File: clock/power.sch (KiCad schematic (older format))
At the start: 51 parts

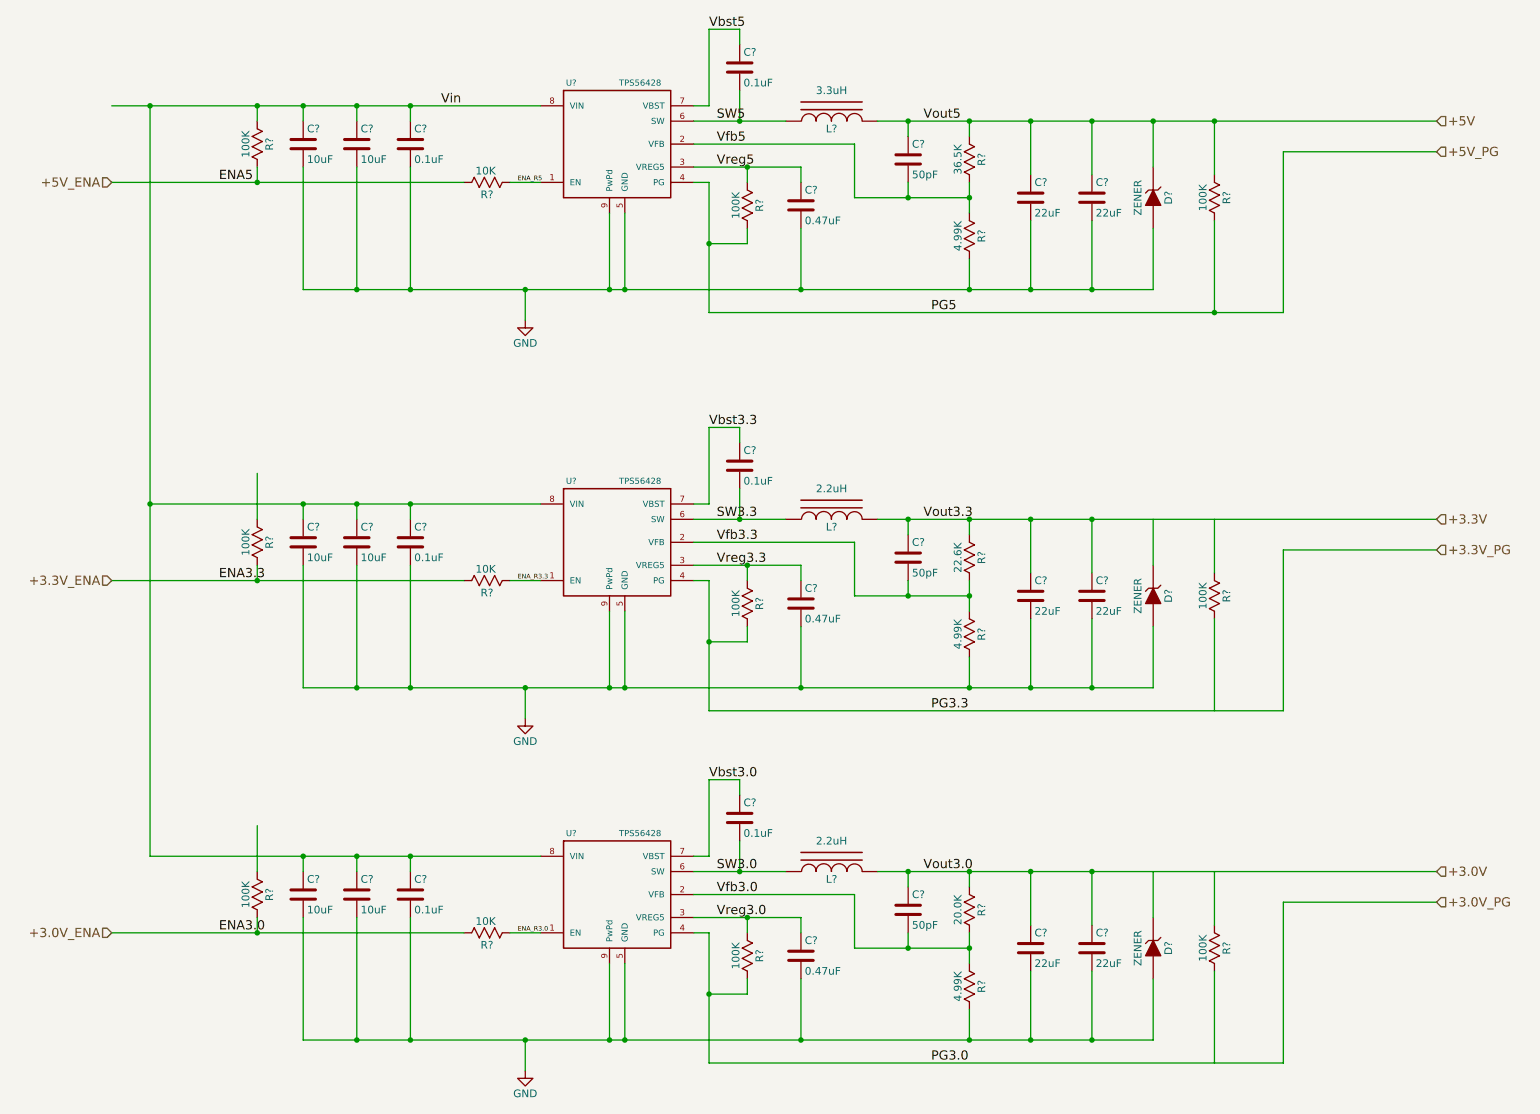
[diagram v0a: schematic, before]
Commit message: Fill in some of the BOM entries.
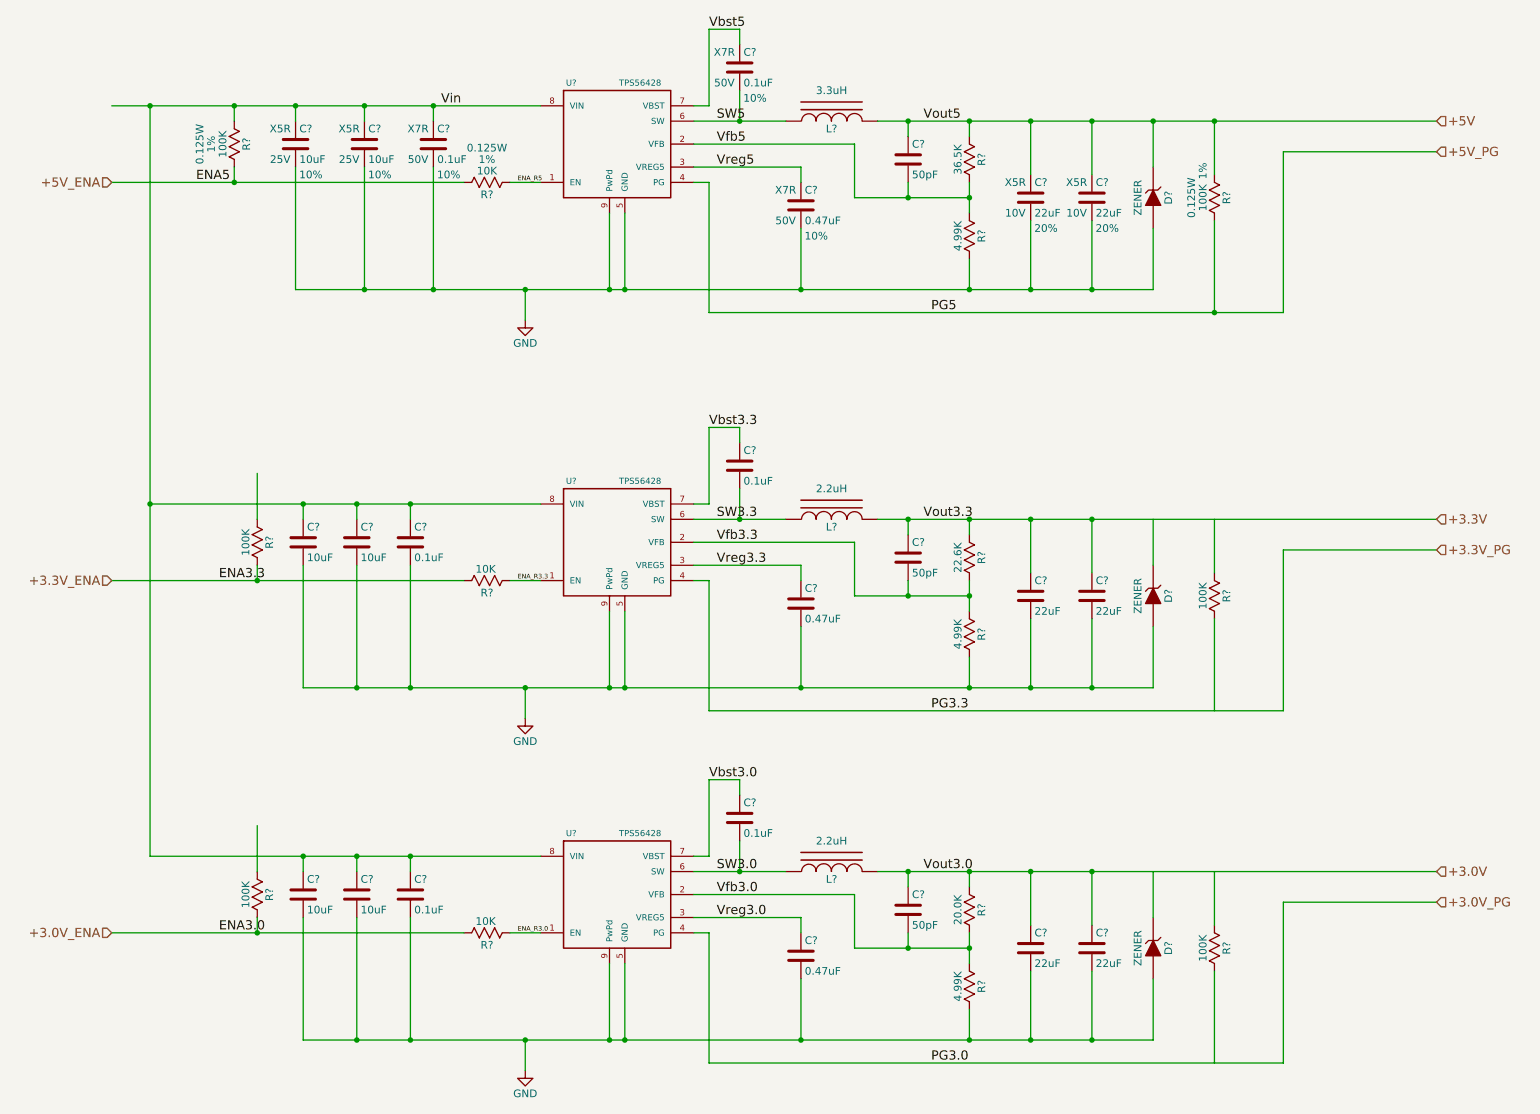
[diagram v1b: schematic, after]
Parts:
- removed C? (x2): 10uF, Capacitors_SMD:C_1206_HandSoldering, symbol C
- removed C? (x2): 0.1uF, Capacitors_SMD:C_0805_HandSoldering, symbol C
- removed C?: 0.47uF, Capacitors_SMD:C_0805_HandSoldering, symbol C
- removed C? (x2): 22uF, Capacitors_SMD:C_1206_HandSoldering, symbol C
- removed R? (x5): 100K, symbol R_local
- removed R?: 10K, symbol R_local
- removed U?: TPS56428, symbol TPS56428
- added C? (x2): 10uF, Capacitors_SMD:C_1206_HandSoldering, symbol C
- added C? (x2): 0.1uF, Capacitors_SMD:C_0805_HandSoldering, symbol C
- added C? (x2): 22uF, Capacitors_SMD:C_1206_HandSoldering, symbol C
- added C?: 0.47uF, Capacitors_SMD:C_0805_HandSoldering, symbol C
- added R? (x2): 100K, Resistors_SMD:R_0805_HandSoldering, symbol R_local
- added R?: 10K, Resistors_SMD:R_0805_HandSoldering, symbol R_local
- added U?: TPS56428, symbol TPS56428
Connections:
- wire segments 148 -> 139

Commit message: Update parts with parameter detail and BOM information.
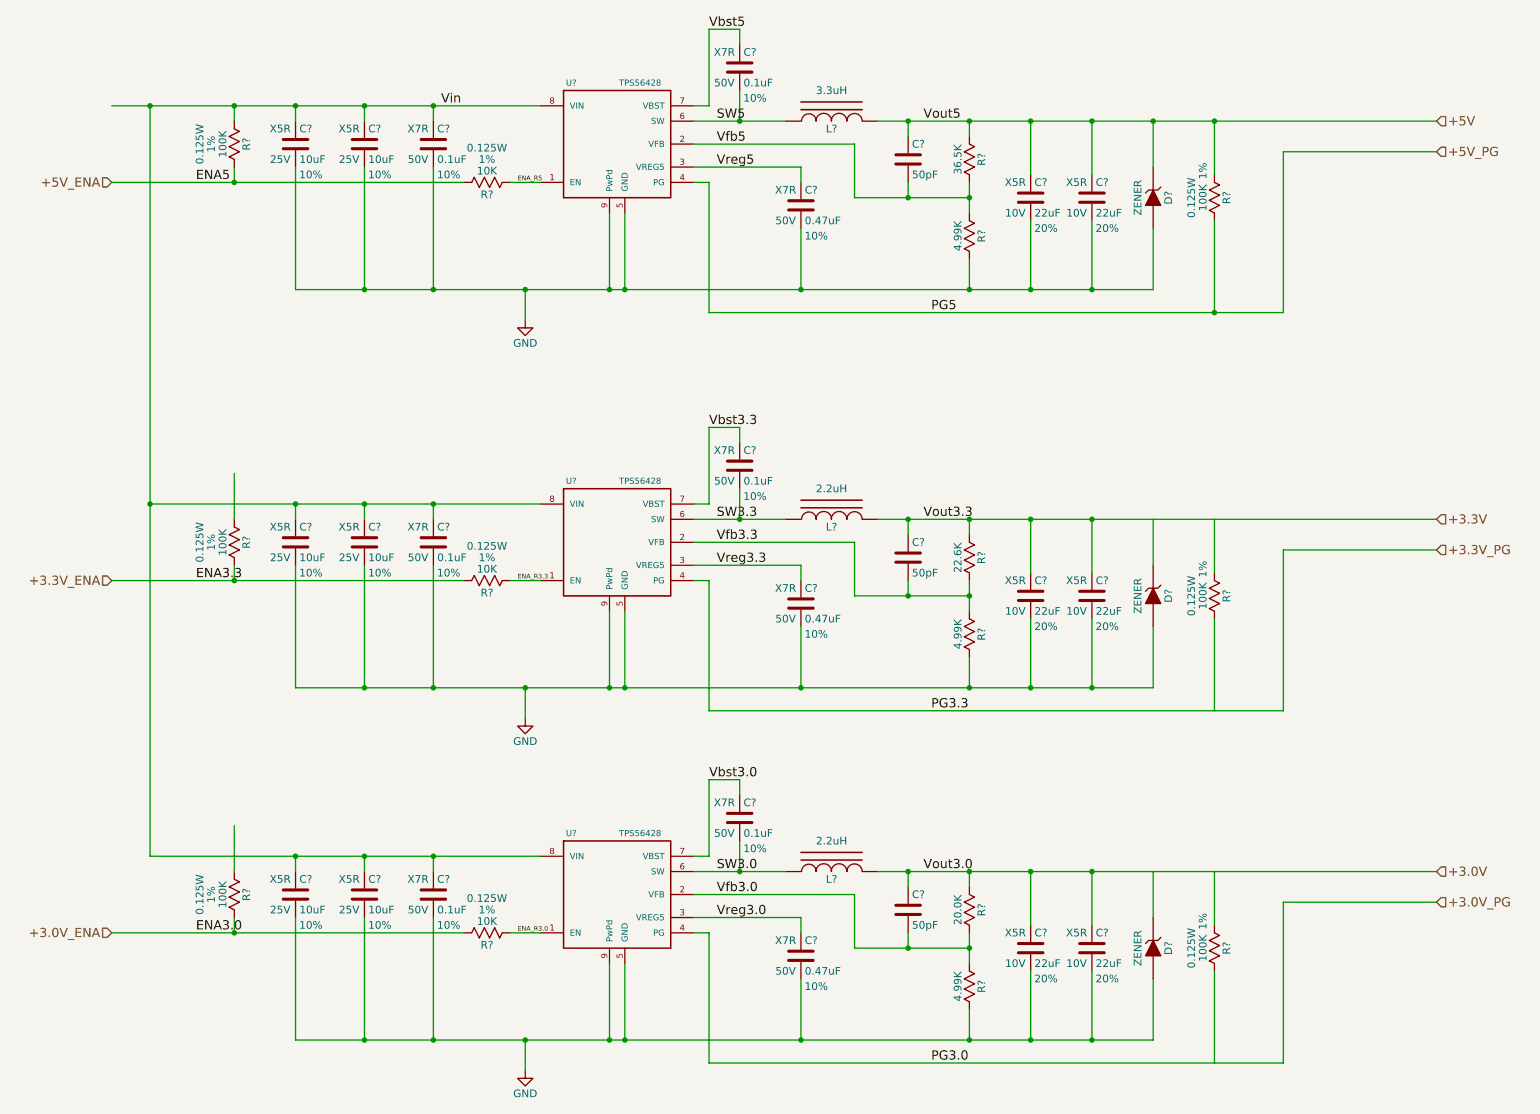
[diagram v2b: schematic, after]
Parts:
- removed C? (x4): 10uF, Capacitors_SMD:C_1206_HandSoldering, symbol C
- removed C? (x4): 0.1uF, Capacitors_SMD:C_0805_HandSoldering, symbol C
- removed C? (x2): 0.47uF, Capacitors_SMD:C_0805_HandSoldering, symbol C
- removed C? (x4): 22uF, Capacitors_SMD:C_1206_HandSoldering, symbol C
- removed R? (x4): 100K, symbol R_local
- removed R? (x2): 10K, symbol R_local
- removed U? (x2): TPS56428, symbol TPS56428
- added C? (x4): 10uF, Capacitors_SMD:C_1206_HandSoldering, symbol C
- added C? (x4): 0.1uF, Capacitors_SMD:C_0805_HandSoldering, symbol C
- added C? (x2): 0.47uF, Capacitors_SMD:C_0805_HandSoldering, symbol C
- added C? (x4): 22uF, Capacitors_SMD:C_1206_HandSoldering, symbol C
- added R? (x2): 10K, Resistors_SMD:R_0805_HandSoldering, symbol R_local
- added R? (x4): 100K, Resistors_SMD:R_0805_HandSoldering, symbol R_local
- added U? (x2): TPS56428, symbol TPS56428
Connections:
- wire segments 139 -> 205

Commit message: Add parameter for RF connector. Start adding display connections.
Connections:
- wire segments 205 -> 139
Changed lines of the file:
@@
 $EndComp
 Wire Wire Line
-	8500 2350 8700 2350
-Wire Wire Line
-	8700 2350 9100 2350
-Wire Wire Line
-	9100 2350 9500 2350
-Wire Wire Line
-	9500 2350 9900 2350
-Wire Wire Line
-	9900 2350 10300 2350
-Wire Wire Line
-	10300 2350 10700 2350
-Wire Wire Line
-	10700 2350 12150 2350
-Wire Wire Line
-	7300 2350 7600 2350
-Wire Wire Line
-	7600 2350 7900 2350
+	8500 2350 12150 2350
+Wire Wire Line
+	7300 2350 7900 2350
 Wire Wire Line
 	7600 2150 7600 2350
@@
 Connection ~ 9900 2350
 Wire Wire Line
-	9100 2750 9100 2850
-Wire Wire Line
-	9100 2850 9100 2950
+	9100 2750 9100 2950
 Wire Wire Line
 	6750 3450 6750 2950
@@
 	9100 3450 9100 3250
 Wire Wire Line
-	8350 2850 8700 2850
-Wire Wire Line
-	8700 2850 9100 2850
+	8350 2850 9100 2850
 Wire Wire Line
 	8350 2850 8350 2500
@@
 Connection ~ 6750 3450
 Wire Wire Line
-	3500 2250 3750 2250
-Wire Wire Line
-	3750 2250 4300 2250
-Wire Wire Line
-	4300 2250 4700 2250
-Wire Wire Line
-	4700 2250 5150 2250
-Wire Wire Line
-	5150 2250 5600 2250
-Wire Wire Line
-	5600 2250 6300 2250
+	3500 2250 6300 2250
 Wire Wire Line
 	6300 2750 6100 2750
 Wire Wire Line
-	3500 2750 4300 2750
-Wire Wire Line
-	4300 2750 5800 2750
-Wire Wire Line
-	7400 3600 10700 3600
-Wire Wire Line
-	10700 3600 11150 3600
+	3500 2750 5800 2750
+Wire Wire Line
+	7400 3600 11150 3600
 Wire Wire Line
 	6850 3450 6850 2950
@@
 $EndComp
 Wire Wire Line
-	8500 4950 8700 4950
-Wire Wire Line
-	8700 4950 9100 4950
-Wire Wire Line
-	9100 4950 9500 4950
-Wire Wire Line
-	9500 4950 9900 4950
-Wire Wire Line
-	9900 4950 12150 4950
-Wire Wire Line
-	7300 4950 7600 4950
-Wire Wire Line
-	7600 4950 7900 4950
+	8500 4950 12150 4950
+Wire Wire Line
+	7300 4950 7900 4950
 Wire Wire Line
 	7600 4750 7600 4950
@@
 Connection ~ 9900 4950
 Wire Wire Line
-	9100 5350 9100 5450
-Wire Wire Line
-	9100 5450 9100 5550
+	9100 5350 9100 5550
 Wire Wire Line
 	6750 6050 6750 5550
 Wire Wire Line
-	4700 6050 5150 6050
-Wire Wire Line
-	5150 6050 5600 6050
-Wire Wire Line
-	5600 6050 6200 6050
-Wire Wire Line
-	6200 6050 6750 6050
-Wire Wire Line
-	6750 6050 6850 6050
-Wire Wire Line
-	6850 6050 8000 6050
-Wire Wire Line
-	8000 6050 9100 6050
-Wire Wire Line
-	9100 6050 9500 6050
-Wire Wire Line
-	9500 6050 9900 6050
-Wire Wire Line
-	9900 6050 10300 6050
+	4700 6050 10300 6050
 Wire Wire Line
 	9100 6050 9100 5850
 Wire Wire Line
-	8350 5450 8700 5450
-Wire Wire Line
-	8700 5450 9100 5450
+	8350 5450 9100 5450
 Wire Wire Line
 	8350 5450 8350 5100
@@
 Connection ~ 6750 6050
 Wire Wire Line
-	3750 4850 4700 4850
-Wire Wire Line
-	4700 4850 5150 4850
-Wire Wire Line
-	5150 4850 5600 4850
-Wire Wire Line
-	5600 4850 6300 4850
+	3750 4850 6300 4850
 Wire Wire Line
 	6300 5350 6100 5350
 Wire Wire Line
-	3500 5350 4300 5350
-Wire Wire Line
-	4300 5350 5800 5350
+	3500 5350 5800 5350
 Wire Wire Line
 	7400 6200 11150 6200
@@
 $EndComp
 Wire Wire Line
-	8500 7250 8700 7250
-Wire Wire Line
-	8700 7250 9100 7250
-Wire Wire Line
-	9100 7250 9500 7250
-Wire Wire Line
-	9500 7250 9900 7250
-Wire Wire Line
-	9900 7250 12150 7250
-Wire Wire Line
-	7300 7250 7600 7250
-Wire Wire Line
-	7600 7250 7900 7250
+	8500 7250 12150 7250
+Wire Wire Line
+	7300 7250 7900 7250
 Wire Wire Line
 	7600 7050 7600 7250
@@
 Connection ~ 9900 7250
 Wire Wire Line
-	9100 7650 9100 7750
-Wire Wire Line
-	9100 7750 9100 7850
+	9100 7650 9100 7850
 Wire Wire Line
 	6750 8350 6750 7850
 Wire Wire Line
-	4700 8350 5150 8350
-Wire Wire Line
-	5150 8350 5600 8350
-Wire Wire Line
-	5600 8350 6200 8350
-Wire Wire Line
-	6200 8350 6750 8350
-Wire Wire Line
-	6750 8350 6850 8350
-Wire Wire Line
-	6850 8350 8000 8350
-Wire Wire Line
-	8000 8350 9100 8350
-Wire Wire Line
-	9100 8350 9500 8350
-Wire Wire Line
-	9500 8350 9900 8350
-Wire Wire Line
-	9900 8350 10300 8350
+	4700 8350 10300 8350
 Wire Wire Line
 	9100 8350 9100 8150
 Wire Wire Line
-	8350 7750 8700 7750
-Wire Wire Line
-	8700 7750 9100 7750
+	8350 7750 9100 7750
 Wire Wire Line
 	8350 7750 8350 7400
@@
 Connection ~ 6750 8350
 Wire Wire Line
-	3750 7150 4700 7150
-Wire Wire Line
-	4700 7150 5150 7150
-Wire Wire Line
-	5150 7150 5600 7150
-Wire Wire Line
-	5600 7150 6300 7150
+	3750 7150 6300 7150
 Wire Wire Line
 	6300 7650 6100 7650
 Wire Wire Line
-	3500 7650 4300 7650
-Wire Wire Line
-	4300 7650 5800 7650
+	3500 7650 5800 7650
 Wire Wire Line
 	7400 8500 11150 8500
@@
 ENA_R3.0
 Wire Wire Line
-	4700 3450 5150 3450
-Wire Wire Line
-	5150 3450 5600 3450
-Wire Wire Line
-	5600 3450 6200 3450
-Wire Wire Line
-	6200 3450 6750 3450
-Wire Wire Line
-	6750 3450 6850 3450
-Wire Wire Line
-	6850 3450 8000 3450
-Wire Wire Line
-	8000 3450 9100 3450
-Wire Wire Line
-	9100 3450 9500 3450
-Wire Wire Line
-	9500 3450 9900 3450
-Wire Wire Line
-	9900 3450 10300 3450
+	4700 3450 10300 3450
 Text HLabel 12150 2350 2    60   Input ~ 0
 +5V
@@
 +3.0V_ENA
 Wire Wire Line
-	3750 2250 3750 4850
-Wire Wire Line
-	3750 4850 3750 7150
+	3750 2250 3750 7150
 Connection ~ 3750 4850
 Connection ~ 3750 2250
